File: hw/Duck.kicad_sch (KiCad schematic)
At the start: 7 parts, among them J1 Conn_01x06, U1 ESP32-S3-MINI-1, U2 SPX3819M5-L-3-3, U3 INMP441

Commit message: hw: Finish schematic
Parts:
- added C3, C4, C6, C7, C9: 100n, Capacitor_SMD:C_0402_1005Metric, symbol Device:C
- added C5: 4.7u, Capacitor_SMD:C_0402_1005Metric, symbol Device:C
- added C8: 1u, Capacitor_SMD:C_0402_1005Metric, symbol Device:C
- added D1: LED_RAGB, LED_THT:LED_D5.0mm-4_RGB, symbol Device:LED_RAGB
- added J2: Conn_01x04, Connector_PinHeader_2.54mm:PinHeader_1x04_P2.54mm_Vertical, symbol Connector_Generic:Conn_01x04
- added J3: USB_C_Receptacle_USB2.0_14P, Connector_USB:USB_C_Receptacle_HRO_TYPE-C-31-M-12, symbol Connector:USB_C_Receptacle_USB2.0_14P
- added Q1, Q2: MMBT3904, Package_TO_SOT_SMD:SOT-23, symbol Transistor_BJT:MMBT3904
- added R1, R2: 4.7k, Resistor_SMD:R_0402_1005Metric, symbol Device:R
- added R3, R4: 5.1k, Resistor_SMD:R_0402_1005Metric, symbol Device:R
- added R5, R6: 10k, Resistor_SMD:R_0402_1005Metric, symbol Device:R
- added U4: MAX17048G+T10, MAX17048G+T10:SON50P200X200X80-9N-D, symbol MAX17048G+T10:MAX17048G+T10
- added U5: CH343P, Package_DFN_QFN:QFN-16-1EP_3x3mm_P0.5mm_EP1.9x1.9mm, symbol CH343:CH343P
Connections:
- net +3V3: now also C4.1, C5.1, C6.1, C7.1, C8.1, D1.2 (A), J2.1 (Pin_1), R1.1, R2.1, U5.1 (VIO), U5.3 (VDD5)
- net +BATT: now also C3.1, U4.3 (VDD)
- net BOOT0: now also Q2.3 (C)
- net ESP_EN: now also Q1.3 (C)
- net GND: now also C3.2, C4.2, C5.2, C6.2, C7.2, C8.2, C9.2, J2.2 (Pin_2), J3.A1 (GND), J3.A12 (GND), J3.B1 (GND), J3.B12 (GND), R3.2, R4.2, U4.1 (CTG), U4.4 (GND), U4.6 (QSTRT), U4.9 (EP), U5.17 (GND), U5.2 (GND)
- net U0RXD: now also U5.4 (TXD)
- net U0TXD: now also U5.5 (RXD)
- net LED_R: now reaches U1.12 (GPIO8/TOUCH8/ADC1_CH7/SUBSPICS1)
- net LED_R: now also D1.1 (RK)
- net LED_G: now reaches U1.13 (GPIO9/TOUCH9/ADC1_CH8/FSPIHD/SUBSPIHD)
- net LED_G: now also D1.3 (GK)
- net LED_B: now reaches U1.14 (GPIO10/TOUCH10/ADC1_CH9/FSPICS0/FSPIIO4/SUBSPICS0)
- net LED_B: now also D1.4 (BK)
- net GNSS_TX: now reaches U1.25 (GPIO21)
- net GNSS_TX: now also J2.3 (Pin_3)
- net GNSS_RX: now reaches U1.26 (GPIO26)
- net GNSS_RX: now also J2.4 (Pin_4)
- net SDA: now reaches U1.8 (GPIO4/TOUCH4/ADC1_CH3)
- net SDA: now also R2.2, U4.8 (SDA)
- net SCL: now reaches U1.9 (GPIO5/TOUCH5/ADC1_CH4)
- net SCL: now also R1.2, U4.7 (SCL)
- new net: Q1.1 (B), R5.2
- new net: C9.1, U5.6 (V3)
- new net: J3.A5 (CC1), R4.1
- new net: J3.B5 (CC2), R3.1
- new net: Q2.1 (B), R6.2
- new net +5V: J3.A4 (VBUS), J3.A9 (VBUS), J3.B4 (VBUS), J3.B9 (VBUS), U5.9 (VBUS)
- new net DTR: Q2.2 (E), R5.1, U5.12 (DTR)
- new net RTS: Q1.2 (E), R6.1, U5.13 (RTS)
- new net USB_D+: J3.A6 (D+), J3.B6 (D+), U5.7 (UD+)
- new net USB_D-: J3.A7 (D-), J3.B7 (D-), U5.8 (UD-)
- no-connect marks 32 -> 33
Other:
- moved on the sheet: U3

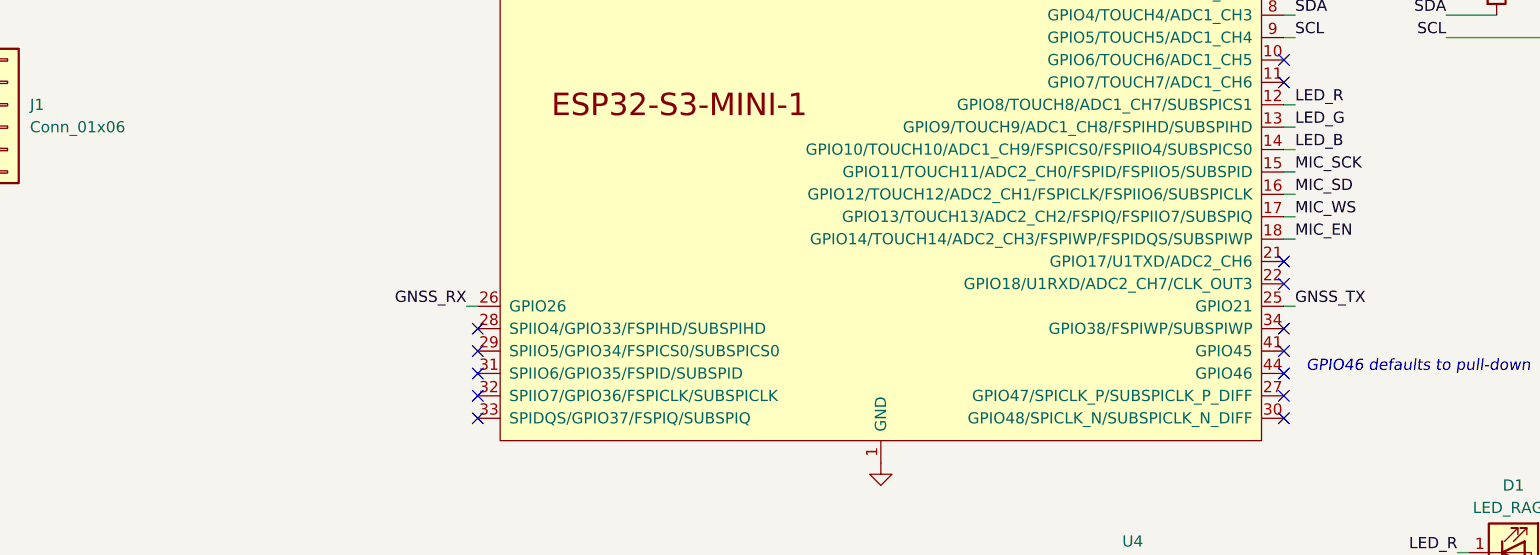
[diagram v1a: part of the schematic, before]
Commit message: hw: Avoid IO26 due to module internal routing
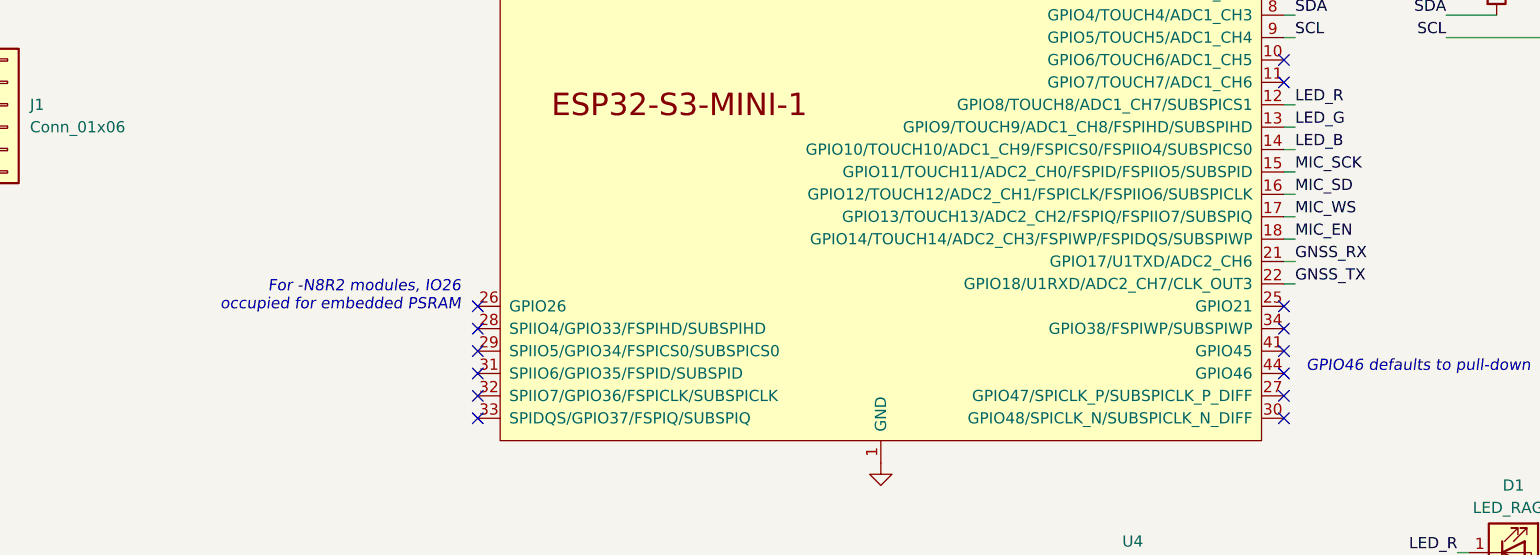
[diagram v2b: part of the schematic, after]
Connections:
- net GNSS_RX: now also U1.21 (GPIO17/U1TXD/ADC2_CH6); no longer U1.26 (GPIO26)
- net GNSS_TX: now also U1.22 (GPIO18/U1RXD/ADC2_CH7/CLK_OUT3); no longer U1.25 (GPIO21)
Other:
- note added: "For -N8R2 modules, IO26 occupied for embedded PSRAM"
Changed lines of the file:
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@@
   (no_connect (at 97.79 93.98))
   (no_connect (at -57.785 69.85))
+  (no_connect (at 97.79 91.44))
   (no_connect (at 97.79 104.14))
-  (no_connect (at 189.23 88.9))
   (no_connect (at 189.23 104.14))
   (no_connect (at 189.23 55.88))
   (no_connect (at 189.23 40.64))
+  (no_connect (at 189.23 91.44))
   (no_connect (at 189.23 101.6))
   (no_connect (at 97.79 99.06))
@@
   (no_connect (at 97.79 50.8))
   (no_connect (at 189.23 43.18))
-  (no_connect (at 189.23 86.36))
   (no_connect (at 97.79 53.34))
   (no_connect (at 189.23 66.04))
@@
     (stroke (width 0) (type default))
   )
-  (wire (pts (xy 96.52 91.44) (xy 97.79 91.44))
+  (wire (pts (xy 190.5 86.36) (xy 189.23 86.36))
     (stroke (width 0) (type default))
   )
@@
     (stroke (width 0) (type default))
   )
-  (wire (pts (xy 190.5 91.44) (xy 189.23 91.44))
+  (wire (pts (xy 190.5 88.9) (xy 189.23 88.9))
     (stroke (width 0) (type default))
   )
@@
     (effects (font (size 1.27 1.27) italic) (justify left bottom))
   )
+  (text "For -N8R2 modules, IO26\noccupied for embedded PSRAM"
+    (at 95.885 92.075 0)
+    (effects (font (size 1.27 1.27) italic) (justify right bottom))
+  )
   (label "SCL" (at 188.595 127.635 0) (fields_autoplaced)
     (effects (font (size 1.27 1.27)) (justify left bottom))
@@
     (effects (font (size 1.27 1.27)) (justify right bottom))
   )
-  (label "GNSS_RX" (at 96.52 91.44 180) (fields_autoplaced)
-    (effects (font (size 1.27 1.27)) (justify right bottom))
-  )
-  (label "GNSS_TX" (at 190.5 91.44 0) (fields_autoplaced)
-    (effects (font (size 1.27 1.27)) (justify left bottom))
-  )
+  (label "GNSS_RX" (at 190.5 86.36 0) (fields_autoplaced)
+    (effects (font (size 1.27 1.27)) (justify left bottom))
+  )
+  (label "GNSS_TX" (at 190.5 88.9 0) (fields_autoplaced)
+    (effects (font (size 1.27 1.27)) (justify left bottom))
+  )

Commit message: hw: Layout
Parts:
- added J4: Conn_01x06, Connector_PinHeader_2.54mm:PinHeader_1x06_P2.54mm_Vertical, symbol Connector_Generic:Conn_01x06
- added JP1: SolderJumper_2_Bridged, Jumper:SolderJumper-2_P1.3mm_Bridged_RoundedPad1.0x1.5mm, symbol Jumper:SolderJumper_2_Bridged
- added R3, R4, R5: 1k, Resistor_SMD:R_0402_1005Metric, symbol Device:R
- J2: footprint Connector_PinHeader_2.54mm:PinHeader_1x04_P2.54mm_Vertical -> Duck_footprints:SMD_1x04_P2.54mm
- J3: footprint Connector_USB:USB_C_Receptacle_HRO_TYPE-C-31-M-12 -> Duck_footprints:USB_C_Receptacle
- renumbered C5 to C1, C6 to C2, C1 to C3, C2 to C4, C4 to C5, C3 to C6, R3 to R6, R4 to R7, R5 to R8, R6 to R9
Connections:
- net +3V3: no longer C7.1, C8.1, U5.1 (VIO), U5.3 (VDD5)
- net +BATT: now also J4.1 (Pin_1), JP1.2 (B)
- net BOOT0: now also J1.6 (Pin_6), J4.6 (Pin_6); no longer J1.4 (Pin_4)
- net ESP_EN: now also J1.5 (Pin_5), J4.5 (Pin_5); no longer J1.3 (Pin_3)
- net GND: now also J4.2 (Pin_2)
- net GNSS_RX: now also U1.13 (GPIO9/TOUCH9/ADC1_CH8/FSPIHD/SUBSPIHD); no longer U1.21 (GPIO17/U1TXD/ADC2_CH6)
- net GNSS_TX: now also U1.12 (GPIO8/TOUCH8/ADC1_CH7/SUBSPICS1); no longer U1.22 (GPIO18/U1RXD/ADC2_CH7/CLK_OUT3)
- net LED_B: now also U1.25 (GPIO21), R5.1; no longer D1.4 (BK), U1.14 (GPIO10/TOUCH10/ADC1_CH9/FSPICS0/FSPIIO4/SUBSPICS0)
- net LED_G: now also U1.22 (GPIO18/U1RXD/ADC2_CH7/CLK_OUT3), R4.1; no longer D1.3 (GK), U1.13 (GPIO9/TOUCH9/ADC1_CH8/FSPIHD/SUBSPIHD)
- net LED_R: now also U1.21 (GPIO17/U1TXD/ADC2_CH6), R3.1; no longer D1.1 (RK), U1.12 (GPIO8/TOUCH8/ADC1_CH7/SUBSPICS1)
- net MIC_EN: now also U1.19 (GPIO15/U0RTS/ADC2_CH4/XTAL_32K_P); no longer U1.18 (GPIO14/TOUCH14/ADC2_CH3/FSPIWP/FSPIDQS/SUBSPIWP)
- net MIC_SCK: now also U1.18 (GPIO14/TOUCH14/ADC2_CH3/FSPIWP/FSPIDQS/SUBSPIWP); no longer U1.15 (GPIO11/TOUCH11/ADC2_CH0/FSPID/FSPIIO5/SUBSPID)
- net MIC_SD: now also U1.17 (GPIO13/TOUCH13/ADC2_CH2/FSPIQ/FSPIIO7/SUBSPIQ); no longer U1.16 (GPIO12/TOUCH12/ADC2_CH1/FSPICLK/FSPIIO6/SUBSPICLK)
- net MIC_WS: now also U1.16 (GPIO12/TOUCH12/ADC2_CH1/FSPICLK/FSPIIO6/SUBSPICLK); no longer U1.17 (GPIO13/TOUCH13/ADC2_CH2/FSPIQ/FSPIIO7/SUBSPIQ)
- net SCL: now also U1.32 (SPIIO7/GPIO36/FSPICLK/SUBSPICLK); no longer U1.9 (GPIO5/TOUCH5/ADC1_CH4)
- net SDA: now also U1.31 (SPIIO6/GPIO35/FSPID/SUBSPID); no longer U1.8 (GPIO4/TOUCH4/ADC1_CH3)
- net U0RXD: now also J1.4 (Pin_4), J4.4 (Pin_4); no longer J1.6 (Pin_6)
- net U0TXD: now also J1.3 (Pin_3), J4.3 (Pin_3); no longer J1.5 (Pin_5)
- net REG_OUT: now reaches C9.1, U5.6 (V3)
- net REG_OUT: now also C7.1, U5.1 (VIO)
- net +5V renamed VBUS
- net VBUS: now also C8.1, U5.3 (VDD5), JP1.1 (A)
- new net: D1.1 (RK), R3.2
- new net: D1.3 (GK), R4.2
- new net: D1.4 (BK), R5.2
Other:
- moved on the sheet: C9, D1

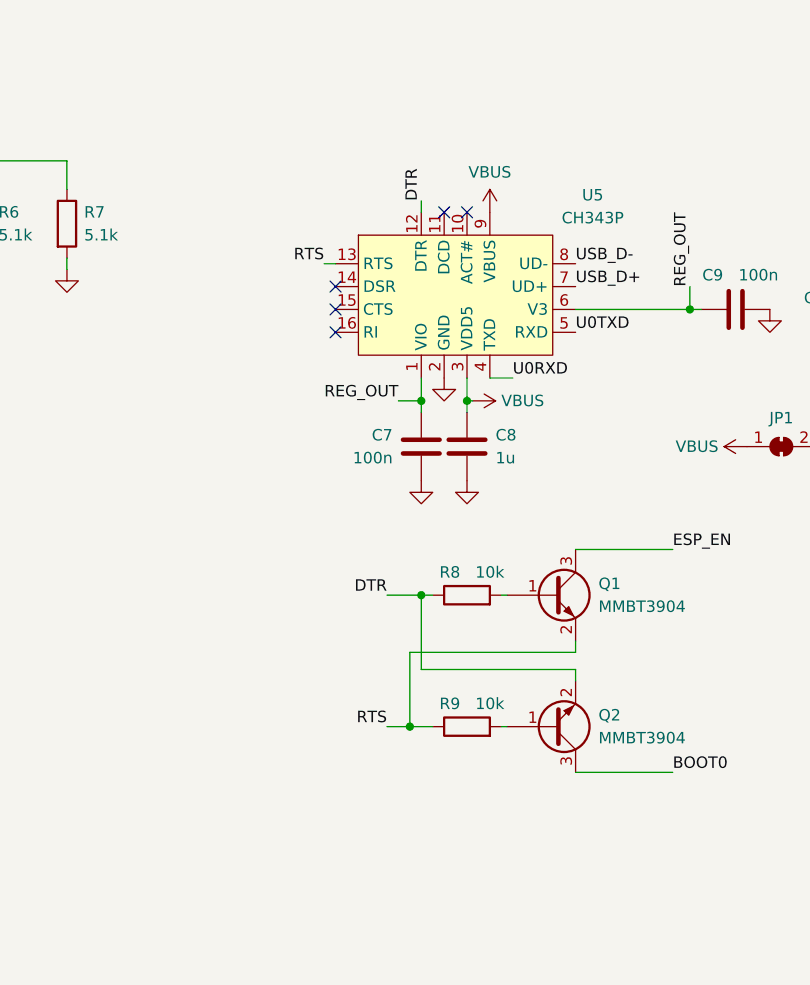
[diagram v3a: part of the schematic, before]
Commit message: hw: Finalize; submit for fab (Rev. 1)
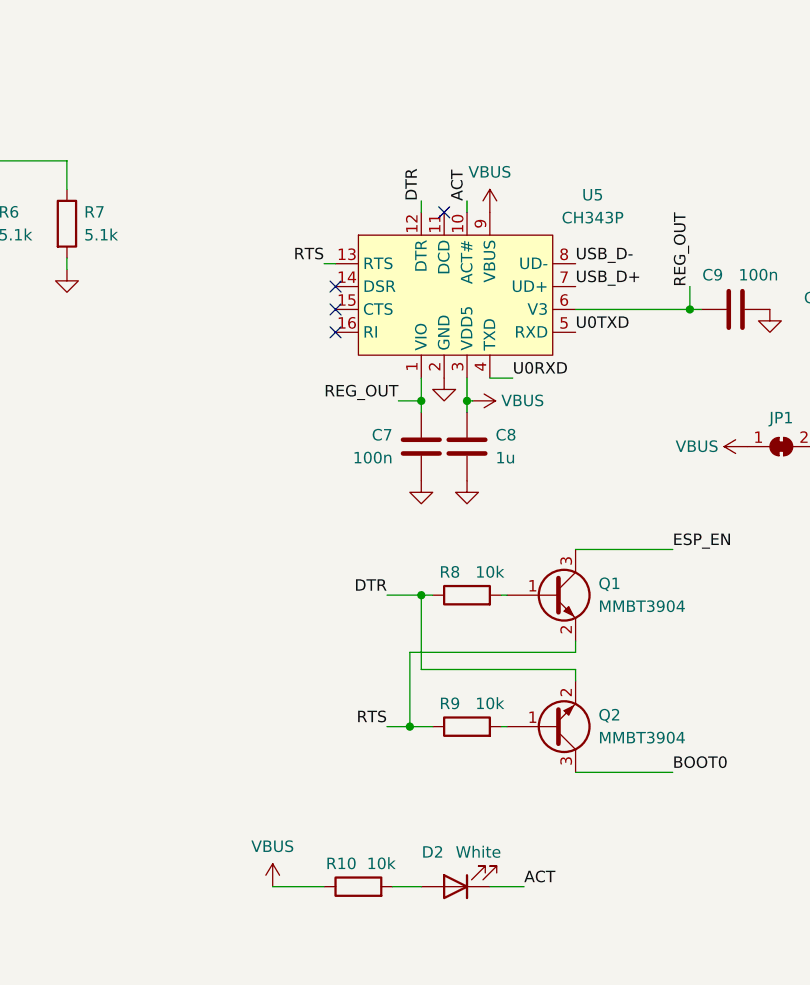
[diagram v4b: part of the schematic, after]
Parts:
- added D2: White, LED_SMD:LED_0603_1608Metric, symbol Device:LED
- added R10: 10k, Resistor_SMD:R_0402_1005Metric, symbol Device:R
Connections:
- net VBUS: now also R10.1
- net ACT: now reaches U5.10 (ACT#)
- net ACT: now also D2.1 (K)
- new net: D2.2 (A), R10.2
- no-connect marks 33 -> 32
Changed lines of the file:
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@@
   (no_connect (at 189.23 99.06))
   (no_connect (at 187.325 132.715))
-  (no_connect (at -43.18 61.595))
   (no_connect (at 189.23 96.52))
   (no_connect (at -45.72 61.595))
@@
     (stroke (width 0) (type default))
   )
+  (wire (pts (xy -51.435 136.525) (xy -48.26 136.525))
+    (stroke (width 0) (type default))
+  )
   (wire (pts (xy 13.97 71.12) (xy 12.7 71.12))
     (stroke (width 0) (type default))
@@
     (stroke (width 0) (type default))
   )
+  (wire (pts (xy -43.18 60.325) (xy -43.18 61.595))
+    (stroke (width 0) (type default))
+  )
   (wire (pts (xy 13.97 68.58) (xy 12.7 68.58))
     (stroke (width 0) (type default))
@@
     (stroke (width 0) (type default))
   )
+  (wire (pts (xy -40.64 136.525) (xy -36.83 136.525))
+    (stroke (width 0) (type default))
+  )
   (wire (pts (xy 62.23 49.53) (xy 52.07 49.53))
     (stroke (width 0) (type default))
@@
   )
   (wire (pts (xy 96.52 101.6) (xy 97.79 101.6))
+    (stroke (width 0) (type default))
+  )
+  (wire (pts (xy -64.77 136.525) (xy -59.055 136.525))
     (stroke (width 0) (type default))
   )
@@
     (effects (font (size 1.27 1.27)) (justify left bottom))
   )
+  (label "ACT" (at -43.18 60.325 90) (fields_autoplaced)
+    (effects (font (size 1.27 1.27)) (justify left bottom))
+  )
   (label "ESP_EN" (at -20.32 99.06 0) (fields_autoplaced)
     (effects (font (size 1.27 1.27)) (justify left bottom))
@@
   )
   (label "U0RXD" (at 190.5 35.56 0) (fields_autoplaced)
+    (effects (font (size 1.27 1.27)) (justify left bottom))
+  )
+  (label "ACT" (at -36.83 136.525 0) (fields_autoplaced)
     (effects (font (size 1.27 1.27)) (justify left bottom))
   )
@@
         (path "/23349607-acbb-4aa4-80bb-d6050790beec"
           (reference "J4") (unit 1)
+        )
+      )
+    )
+  )
+  (symbol (lib_id "power:VBUS") (at -64.77 136.525 0) (unit 1)
+    (in_bom yes) (on_board yes) (dnp no) (fields_autoplaced)
+    (property "Reference" "#PWR037" (at -64.77 140.335 0)
+      (effects (font (size 1.27 1.27)) hide)
+    )
+    (property "Value" "VBUS" (at -64.77 132.08 0)
+      (effects (font (size 1.27 1.27)))
+    )
+    (property "Footprint" "" (at -64.77 136.525 0)
+      (effects (font (size 1.27 1.27)) hide)
+    )
+    (property "Datasheet" "" (at -64.77 136.525 0)
+      (effects (font (size 1.27 1.27)) hide)
+    )
+    (pin "1")
+    (instances
+      (project "Duck"
+        (path "/23349607-acbb-4aa4-80bb-d6050790beec"
+          (reference "#PWR037") (unit 1)
         )
       )
@@
     )
   )
+  (symbol (lib_id "Device:R") (at -55.245 136.525 90) (unit 1)
+    (in_bom yes) (on_board yes) (dnp no)
+    (property "Reference" "R10" (at -57.15 133.985 90)
+      (effects (font (size 1.27 1.27)))
+    )
+    (property "Value" "10k" (at -52.705 133.985 90)
+      (effects (font (size 1.27 1.27)))
+    )
+    (property "Footprint" "Resistor_SMD:R_0402_1005Metric" (at -55.245 138.303 90)
+      (effects (font (size 1.27 1.27)) hide)
+    )
+    (property "Datasheet" "~" (at -55.245 136.525 0)
+      (effects (font (size 1.27 1.27)) hide)
+    )
+    (pin "2")
+    (pin "1")
+    (instances
+      (project "Duck"
+        (path "/23349607-acbb-4aa4-80bb-d6050790beec"
+          (reference "R10") (unit 1)
+        )
+      )
+    )
+  )
   (symbol (lib_id "Device:Battery_Cell") (at 22.86 46.355 0) (mirror y) (unit 1)
     (in_bom yes) (on_board yes) (dnp no)
@@
         )
       )
+    )
+  )
+  (symbol (lib_id "Device:LED") (at -44.45 136.525 180) (unit 1)
+    (in_bom yes) (on_board yes) (dnp no)
+    (property "Reference" "D2" (at -46.99 132.715 0)
+      (effects (font (size 1.27 1.27)))
+    )
+    (property "Value" "White" (at -41.91 132.715 0)
+      (effects (font (size 1.27 1.27)))
+    )
+    (property "Footprint" "LED_SMD:LED_0603_1608Metric" (at -44.45 136.525 0)
+      (effects (font (size 1.27 1.27)) hide)
+    )
+    (property "Datasheet" "~" (at -44.45 136.525 0)
+      (effects (font (size 1.27 1.27)) hide)
+    )
+    (pin "1")
+    (pin "2")
+    (instances
+      (project "Duck"
+        (path "/23349607-acbb-4aa4-80bb-d6050790beec"
+          (reference "D2") (unit 1)
+        )
+      )

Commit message: hw: 🚧 Revision
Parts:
- removed U1: ESP32-S3-MINI-1, Espressif:ESP32-S3-MINI-1, symbol Espressif:ESP32-S3-MINI-1
- added AE1: 2.4GHz 50R, Duck_footprints:ANT_IFA_USB_2.4GHz_50R, symbol Device:Antenna_Dipole
- added C3: 1u, Capacitor_SMD:C_0402_1005Metric, symbol Device:C
- added C4, C5: 0 TBD, Capacitor_SMD:C_0402_1005Metric, symbol Device:C
- added C6: 100n, Capacitor_SMD:C_0402_1005Metric, symbol Device:C
- added C7, C8: 6.8p, Capacitor_SMD:C_0402_1005Metric, symbol Device:C
- added L1: 0 TBD, Inductor_SMD:L_0402_1005Metric, symbol Device:L
- added R1: 10k, Resistor_SMD:R_0402_1005Metric, symbol Device:R
- added U1: ESP32-S3-PICO-1, Espressif:ESP32-S3-PICO-1-LGA-56, symbol Espressif:ESP32-S3-PICO-1
- added U2: PY32F003F1xU6, Package_DFN_QFN:QFN-20-1EP_3x3mm_P0.4mm_EP1.65x1.65mm, symbol PY32F003:PY32F003F1xU6
- added Y1: 32MHz 12pF, Crystal:Crystal_SMD_2016-4Pin_2.0x1.6mm, symbol Device:Crystal_GND24
- D1: footprint LED_THT:LED_D5.0mm-4_RGB -> Duck_footprints:LED_1x04_D5.0_P1.27
- J2: footprint Duck_footprints:SMD_1x04_P2.54mm -> Duck_footprints:TestPoints_1x04_P2.0
- renumbered C4 to C10, C5 to C11, C6 to C12, C7 to C13, C8 to C14, C9 to C15, C3 to C9, R9 to R10, R10 to R11, R1 to R2, R2 to R3, R3 to R4, R4 to R5, R5 to R6, R6 to R7, R7 to R8, R8 to R9, U2 to U3, U3 to U4, U4 to U5, U5 to U6
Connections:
- net MIC_EN is gone; now on net +3V3: U4.8 (EN)
- net +3V3: now also C6.1, R1.1, U1.2 (VDD), U1.20 (VDD_RTC), U1.3 (VDD), U1.55 (VDDA), U1.56 (VDDA), U2.6 (VCC)
- net BOOT0: now also U1.5 (GPIO0/BOOT)
- net ESP_EN: now also C3.1, R1.2, U1.4 (EN)
- net GND: now also AE1.2, C3.2, C4.2, C5.2, C6.2, C7.2, C8.2, U1.57 (GND), U2.21 (PAD), U2.4 (VSS), Y1.2, Y1.4
- net LED_B: now also U2.2 (PA6)
- net LED_G: now also U2.20 (PA4)
- net LED_R: now also U2.1 (PA5)
- net MIC_SCK: now also U2.17 (PA1)
- net MIC_SD: now also U2.16 (PA0)
- net MIC_WS: now also U2.3 (PA7)
- net SCL: now also U2.19 (PA3)
- net SDA: now also U2.18 (PA2)
- net U0RXD: now also U1.50 (U0RXD/GPIO44)
- net U0TXD: now also U1.49 (U0TXD/GPIO43)
- net GNSS_RX renamed SWCLK
- net SWCLK: now also U2.8 (PA14)
- net GNSS_TX renamed SWDIO
- net SWDIO: now also U2.7 (PA13)
- new net: AE1.1, C4.1, L1.1
- new net: C5.1, L1.2, U1.1 (LNA_IN)
- new net: C7.1, U2.14 (PF1), Y1.3
- new net: C8.1, U2.13 (PF0), Y1.1
- new net SER_DN: U1.40 (GPIO35), U2.11 (PB7)
- new net SER_UP: U1.39 (GPIO34), U2.10 (PB6)
- no-connect marks 32 -> 46
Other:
- note added: "I2C_SCL"
- note added: "I2C_SDA"
- note added: "SPI1_MISO"
- note added: "SPI1_SCK"
- note added: "TIM17_CH1"
- note added: "TIM3_CH1"
- note added: "TIM3_CH2"
- note added: "TIM3_CH3"
- note added: "USART1_RX"
- note added: "USART1_TX"
- note removed: "For -N8R2 modules, IO26 occupied for embedded PSRAM"
- note removed: "GPIO46 defaults to pull-down"
- moved on the sheet: C1, C11, C12, C2, D1, R4, R5, R6, U4, U5

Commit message: hw: 🚧 Adjustments; layout?
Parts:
- removed C4, C5: 0 TBD, Capacitor_SMD:C_0402_1005Metric, symbol Device:C
- removed L1: 0 TBD, Inductor_SMD:L_0402_1005Metric, symbol Device:L
- removed R2, R3: 4.7k, Resistor_SMD:R_0402_1005Metric, symbol Device:R
- Y1: value 32MHz 12pF -> 24.576MHz 12pF
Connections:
- net +3V3: no longer U4.4 (L/R)
- net GND: now also U4.4 (L/R)
- net LED_B: now also U2.1 (PA5); no longer U2.2 (PA6)
- net LED_R: now also U2.18 (PA2); no longer U2.1 (PA5)
- net MIC_SCK: now also U2.10 (PB6); no longer U2.17 (PA1)
- net MIC_SD: now also U2.2 (PA6); no longer U2.16 (PA0)
- net SCL: now also U2.15 (PF2); no longer U2.19 (PA3)
- net SDA: now also U2.12 (PF4); no longer U2.18 (PA2)
- net SER_DN: now also U1.27 (GPIO21), U2.17 (PA1); no longer U1.40 (GPIO35), U2.11 (PB7)
- net SER_UP: now also U1.36 (GPIO48/SPICLK_N), U2.16 (PA0); no longer U1.39 (GPIO34), U2.10 (PB6)
- net at AE1.1: now also U1.1 (LNA_IN)
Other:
- note added: "TIM16_CH1N"
- note added: "USART2_RX"
- note added: "USART2_TX"
- note removed: "I2C_SCL"
- note removed: "I2C_SDA"
- note removed: "SPI1_SCK"
- note removed: "USART1_RX"
- note removed: "USART1_TX"
- moved on the sheet: AE1, J2
